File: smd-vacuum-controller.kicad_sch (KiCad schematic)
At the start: 4 parts

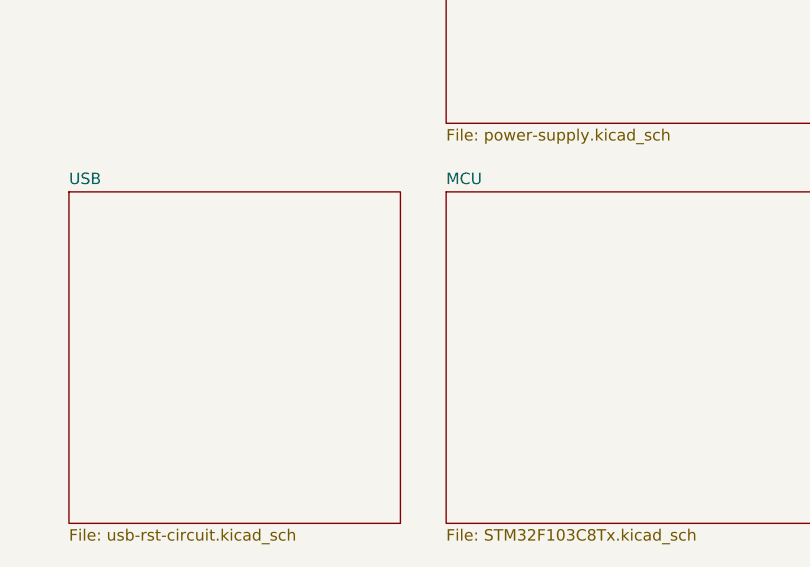
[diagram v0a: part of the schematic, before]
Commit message: Added footwitch, usb led activity
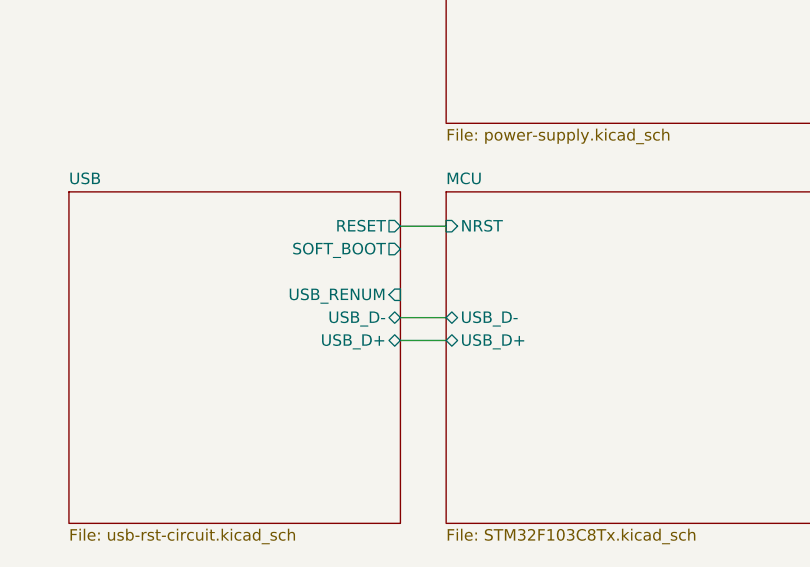
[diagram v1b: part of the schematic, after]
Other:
- sheet MCU ports: added NRST, USB_D+, USB_D-; removed none
- sheet USB ports: added RESET, SOFT_BOOT, USB_D+, USB_D-, USB_RENUM; removed none
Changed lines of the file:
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@@
+	(wire
+		(pts
+			(xy 115.57 102.87) (xy 120.65 102.87)
+		)
+		(stroke
+			(width 0)
+			(type default)
+		)
+	)
 	(wire
 		(pts
@@
 	(wire
 		(pts
+			(xy 115.57 90.17) (xy 120.65 90.17)
+		)
+		(stroke
+			(width 0)
+			(type default)
+		)
+	)
+	(wire
+		(pts
 			(xy 57.15 172.72) (xy 57.15 182.88)
+		)
+		(stroke
+			(width 0)
+			(type default)
+		)
+	)
+	(wire
+		(pts
+			(xy 115.57 100.33) (xy 120.65 100.33)
 		)
 		(stroke
@@
 			)
 		)
+		(pin "USB_D+" bidirectional
+			(at 120.65 102.87 180)
+			(effects
+				(font
+					(size 1.27 1.27)
+				)
+				(justify left)
+			)
+		)
+		(pin "USB_D-" bidirectional
+			(at 120.65 100.33 180)
+			(effects
+				(font
+					(size 1.27 1.27)
+				)
+				(justify left)
+			)
+		)
+		(pin "NRST" input
+			(at 120.65 90.17 180)
+			(effects
+				(font
+					(size 1.27 1.27)
+				)
+				(justify left)
+			)
+		)
 		(instances
 			(project "smd-vacuum-controller"
@@
 			)
 		)
+		(pin "RESET" output
+			(at 115.57 90.17 0)
+			(effects
+				(font
+					(size 1.27 1.27)
+				)
+				(justify right)
+			)
+		)
+		(pin "USB_RENUM" input
+			(at 115.57 97.79 0)
+			(effects
+				(font
+					(size 1.27 1.27)
+				)
+				(justify right)
+			)
+		)
+		(pin "USB_D-" bidirectional
+			(at 115.57 100.33 0)
+			(effects
+				(font
+					(size 1.27 1.27)
+				)
+				(justify right)
+			)
+		)
+		(pin "USB_D+" bidirectional
+			(at 115.57 102.87 0)
+			(effects
+				(font
+					(size 1.27 1.27)
+				)
+				(justify right)
+			)
+		)
+		(pin "SOFT_BOOT" output
+			(at 115.57 92.71 0)
+			(effects
+				(font
+					(size 1.27 1.27)
+				)
+				(justify right)
+			)
+		)

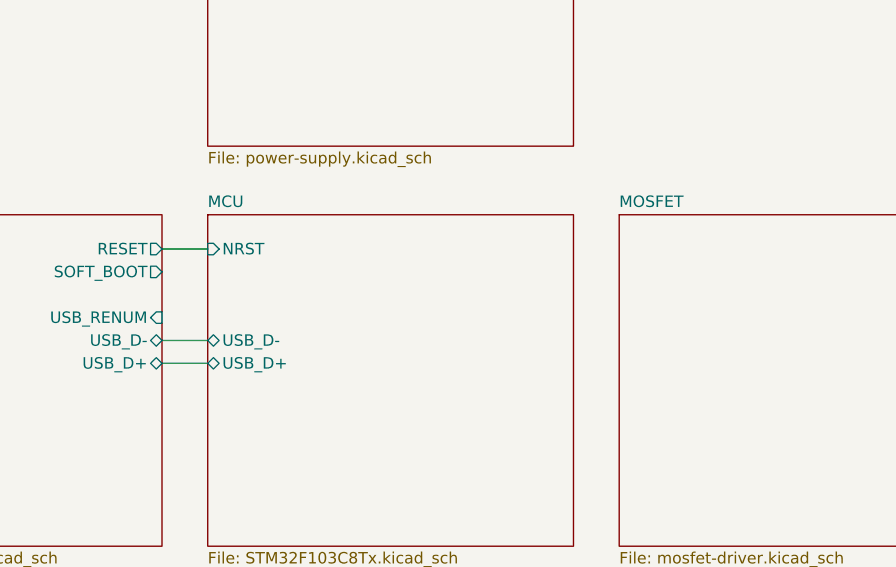
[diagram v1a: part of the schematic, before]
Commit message: Added push button connector
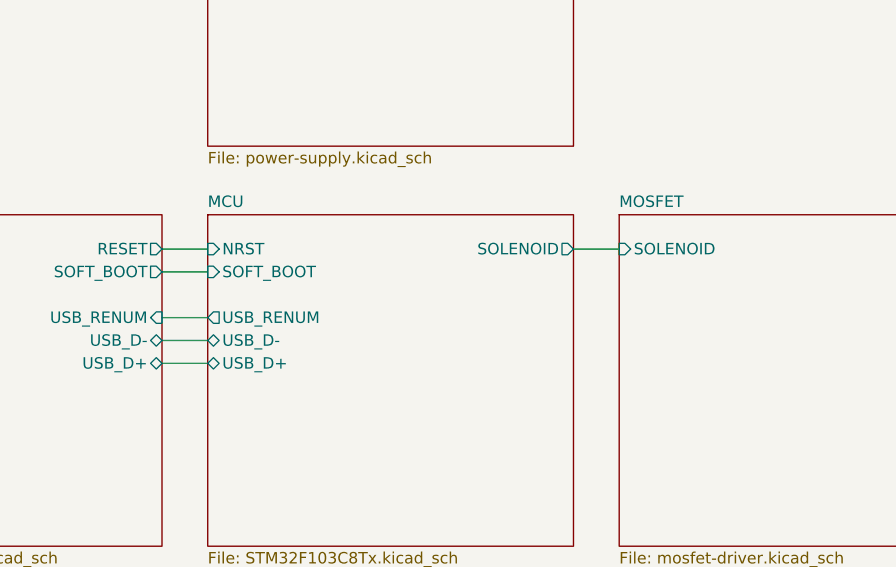
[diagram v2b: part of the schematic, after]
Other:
- sheet MCU ports: added SOFT_BOOT, SOLENOID, USB_RENUM; removed none
- sheet MOSFET ports: added SOLENOID; removed none
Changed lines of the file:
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@@
+	(wire
+		(pts
+			(xy 115.57 92.71) (xy 120.65 92.71)
+		)
+		(stroke
+			(width 0)
+			(type default)
+		)
+	)
 	(wire
 		(pts
@@
 	(wire
 		(pts
+			(xy 161.29 90.17) (xy 166.37 90.17)
+		)
+		(stroke
+			(width 0)
+			(type default)
+		)
+	)
+	(wire
+		(pts
 			(xy 27.94 172.72) (xy 35.56 172.72)
 		)
@@
 		(pts
 			(xy 115.57 100.33) (xy 120.65 100.33)
+		)
+		(stroke
+			(width 0)
+			(type default)
+		)
+	)
+	(wire
+		(pts
+			(xy 115.57 97.79) (xy 120.65 97.79)
 		)
 		(stroke
@@
 			)
 		)
+		(pin "SOFT_BOOT" input
+			(at 120.65 92.71 180)
+			(effects
+				(font
+					(size 1.27 1.27)
+				)
+				(justify left)
+			)
+		)
+		(pin "SOLENOID" output
+			(at 161.29 90.17 0)
+			(effects
+				(font
+					(size 1.27 1.27)
+				)
+				(justify right)
+			)
+		)
+		(pin "USB_RENUM" output
+			(at 120.65 97.79 180)
+			(effects
+				(font
+					(size 1.27 1.27)
+				)
+				(justify left)
+			)
+		)
 		(instances
 			(project "smd-vacuum-controller"
@@
 			)
 		)
+		(pin "SOLENOID" input
+			(at 166.37 90.17 180)
+			(effects
+				(font
+					(size 1.27 1.27)
+				)
+				(justify left)
+			)
+		)
